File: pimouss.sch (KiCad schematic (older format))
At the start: 20 parts

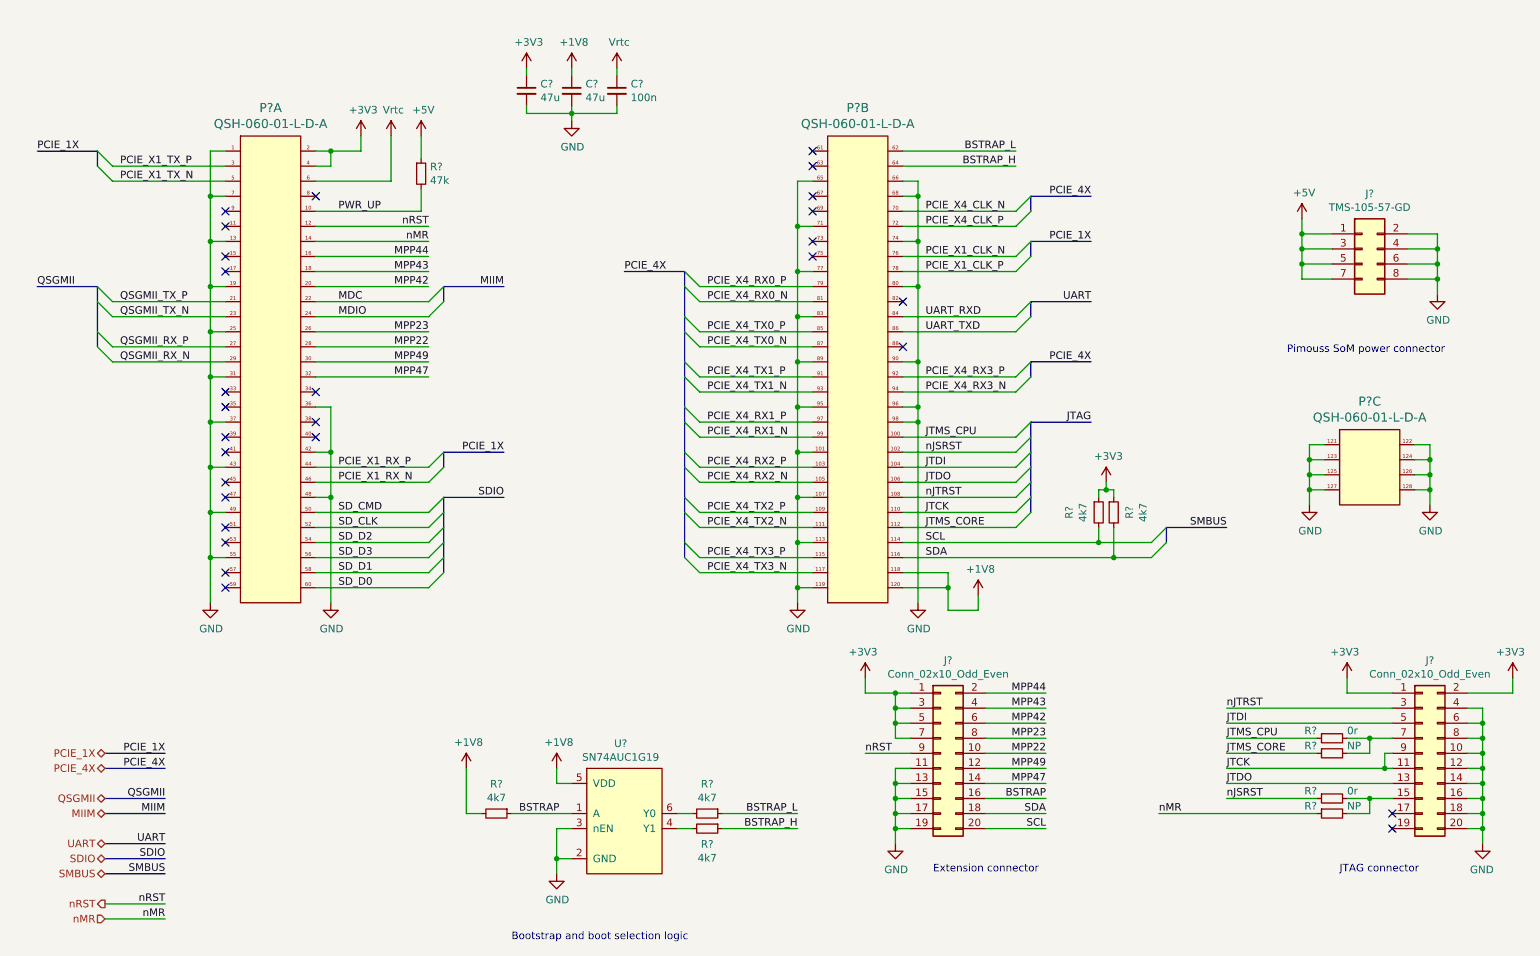
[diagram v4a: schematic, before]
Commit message: sch: Remove ALL busses since kicad's support is broken
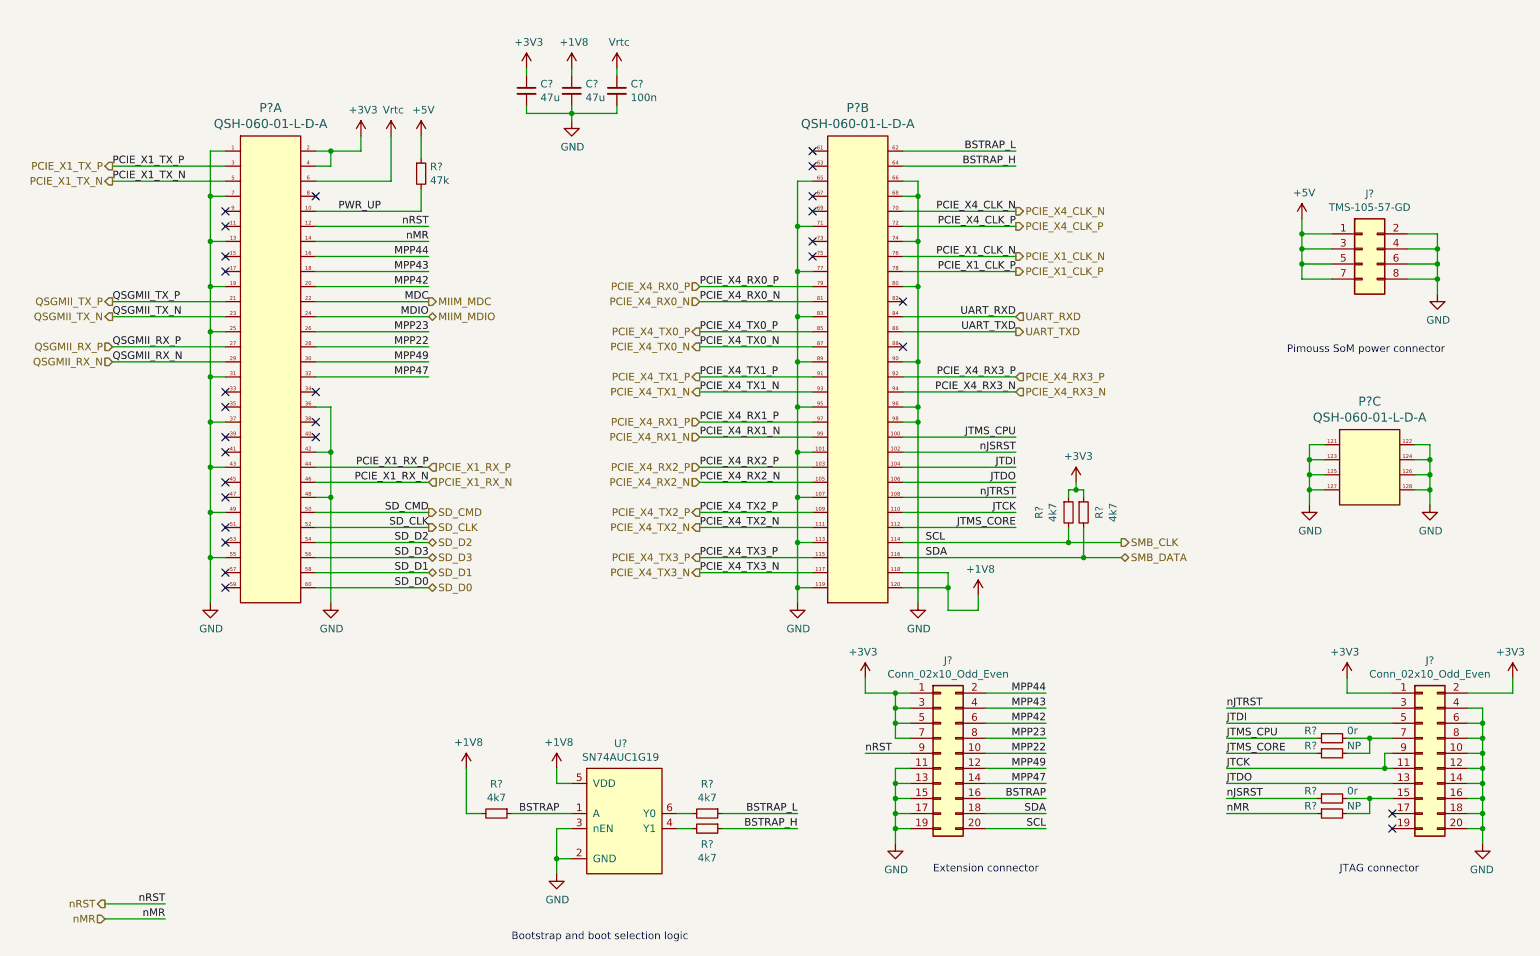
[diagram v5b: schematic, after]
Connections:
- net MDC renamed MIIM_MDC
- net MDIO renamed MIIM_MDIO
- net SCL renamed SMB_CLK
- net SDA renamed SMB_DATA
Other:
- moved on the sheet: R?

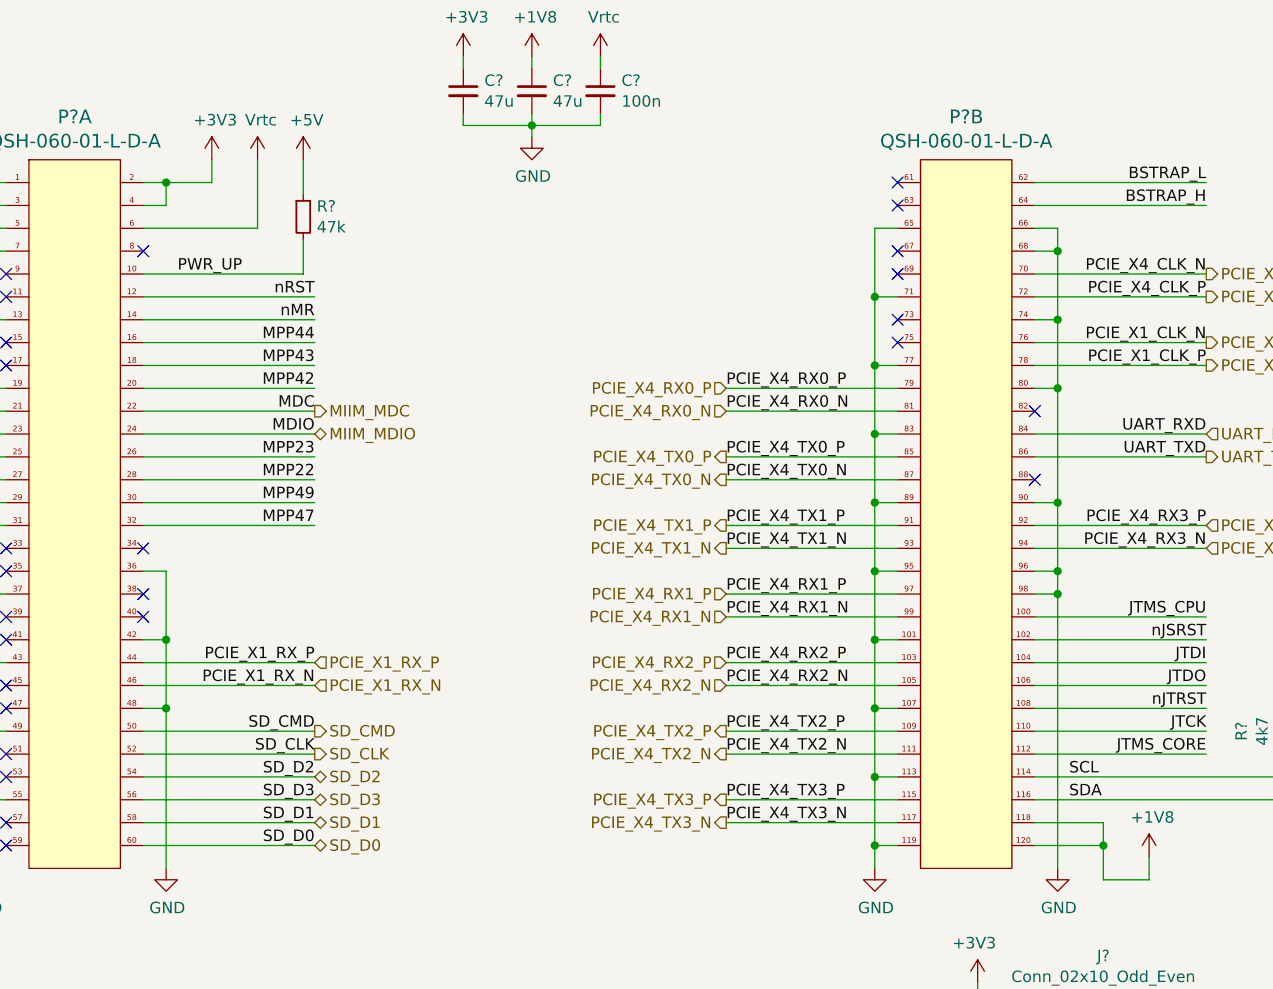
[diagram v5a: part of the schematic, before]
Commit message: sch: Make ERC happy with dummy power outputs
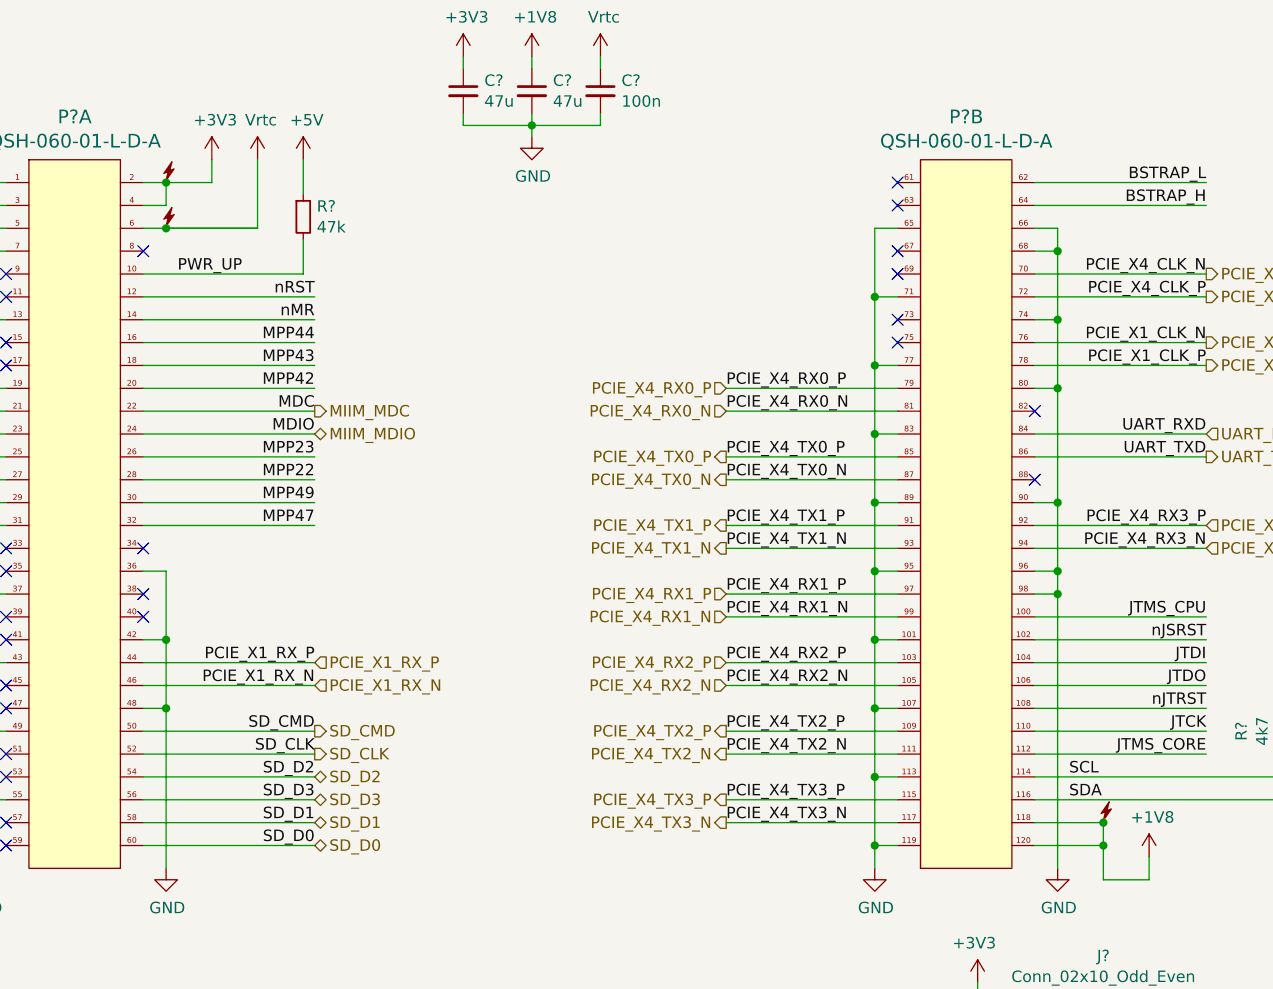
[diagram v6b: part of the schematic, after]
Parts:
- added DS? (x3): DummySupply, symbol pimouss-motherboard:DummySupply
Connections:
- net +1V8: now also DS?.~ (Dummy)
- net +3V3: now also DS?.~ (Dummy)
- net Vrtc: now also DS?.~ (Dummy)
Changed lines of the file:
@@
 Text HLabel 1550 1700 0    50   Output ~ 0
 PCIE_X1_TX_P
+$Comp
+L pimouss-motherboard:DummySupply DS?
+U 1 1 5DE0B5A3
+P 7100 4400
+AR Path="/5DE0B5A3" Ref="DS?"  Part="1"
+AR Path="/5CE77C37/5DE0B5A3" Ref="DS?"  Part="1"
+F 0 "DS?" H 7100 4400 50  0001 C CNN
+F 1 "DummySupply" H 7100 4400 50  0001 C CNN
+F 2 "" H 7100 4400 50  0001 C CNN
+F 3 "" H 7100 4400 50  0001 C CNN
+	1    7100 4400
+	1    0    0    -1
+$EndComp
+$Comp
+L pimouss-motherboard:DummySupply DS?
+U 1 1 5DE20D38
+P 3000 1800
+AR Path="/5DE20D38" Ref="DS?"  Part="1"
+AR Path="/5CE77C37/5DE20D38" Ref="DS?"  Part="1"
+F 0 "DS?" H 3000 1800 50  0001 C CNN
+F 1 "DummySupply" H 3000 1800 50  0001 C CNN
+F 2 "" H 3000 1800 50  0001 C CNN
+F 3 "" H 3000 1800 50  0001 C CNN
+	1    3000 1800
+	1    0    0    -1
+$EndComp
+$Comp
+L pimouss-motherboard:DummySupply DS?
+U 1 1 5DE48D70
+P 3000 1600
+AR Path="/5DE48D70" Ref="DS?"  Part="1"
+AR Path="/5CE77C37/5DE48D70" Ref="DS?"  Part="1"
+F 0 "DS?" H 3000 1600 50  0001 C CNN
+F 1 "DummySupply" H 3000 1600 50  0001 C CNN
+F 2 "" H 3000 1600 50  0001 C CNN
+F 3 "" H 3000 1600 50  0001 C CNN
+	1    3000 1600
+	1    0    0    -1
+$EndComp
+Connection ~ 3000 1800
+Wire Wire Line
+	3000 1800 3400 1800
+Connection ~ 7100 4400
 $EndSCHEMATC

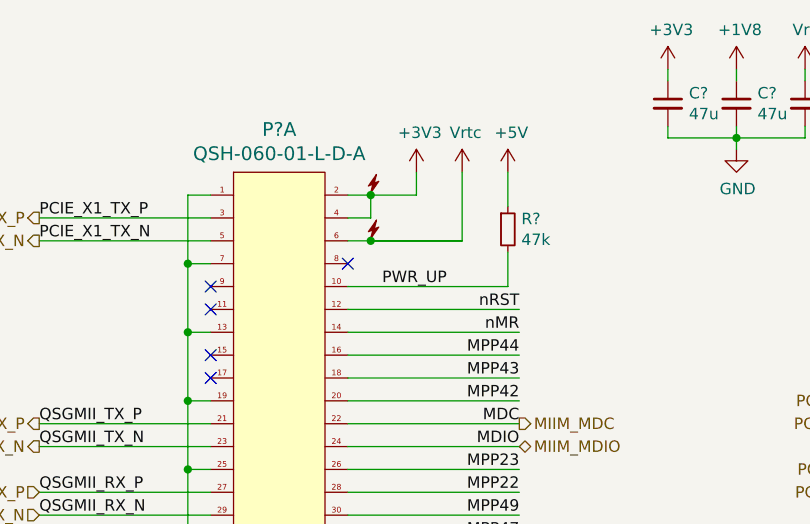
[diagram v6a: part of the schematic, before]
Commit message: lib, sch: Misc changes to make ERC happy
- add resistors to PCIe switch GPIOs
- add NC flags on PHY unused LED outputs
- add dummy supply on Earth PSU
- add dummy supply on PHY ref clock's VCC
- LTC3633: deduplicate SW1/2 outputs
- ILS8033: deduplicate LX1/2 and PGND1/2 outputs
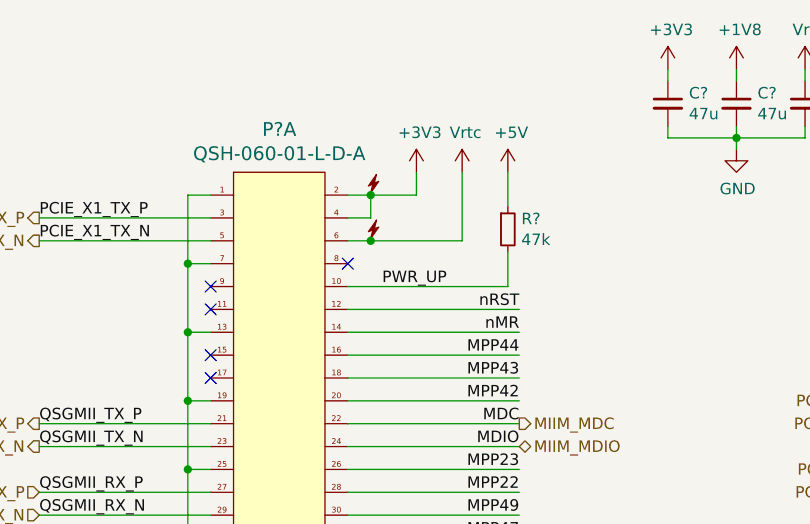
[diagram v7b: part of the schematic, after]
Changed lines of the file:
@@
 $EndComp
 Wire Wire Line
-	2900 1800 3400 1800
+	2900 1800 3000 1800
 Wire Wire Line
 	3400 1800 3400 1500

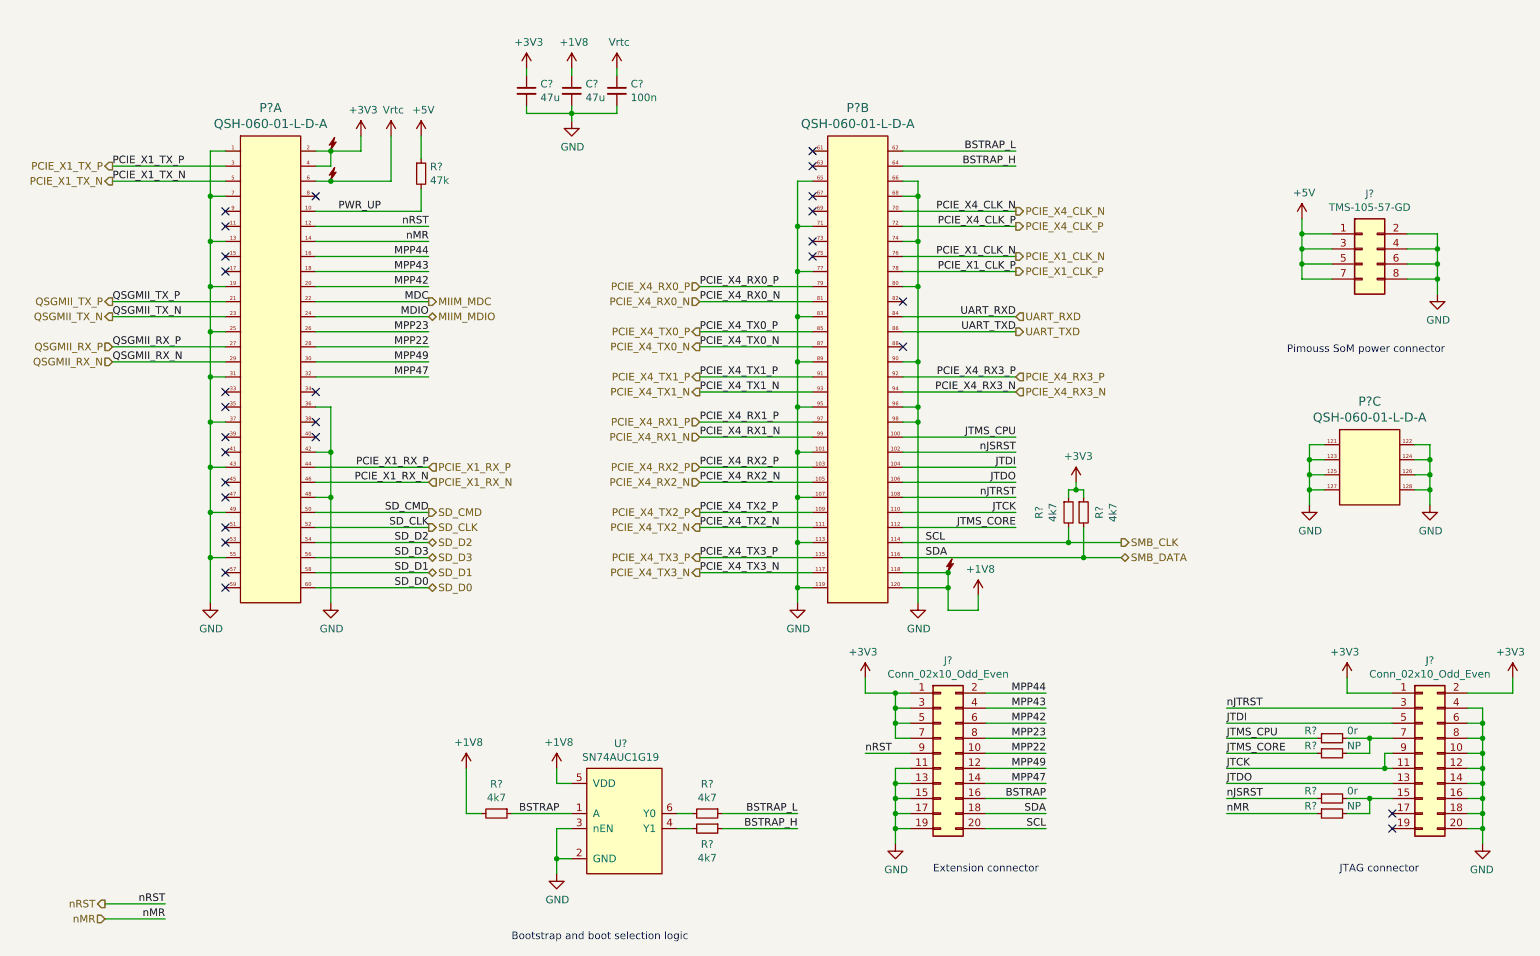
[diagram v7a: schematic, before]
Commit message: sch: Annotate & associate symbols with footprints
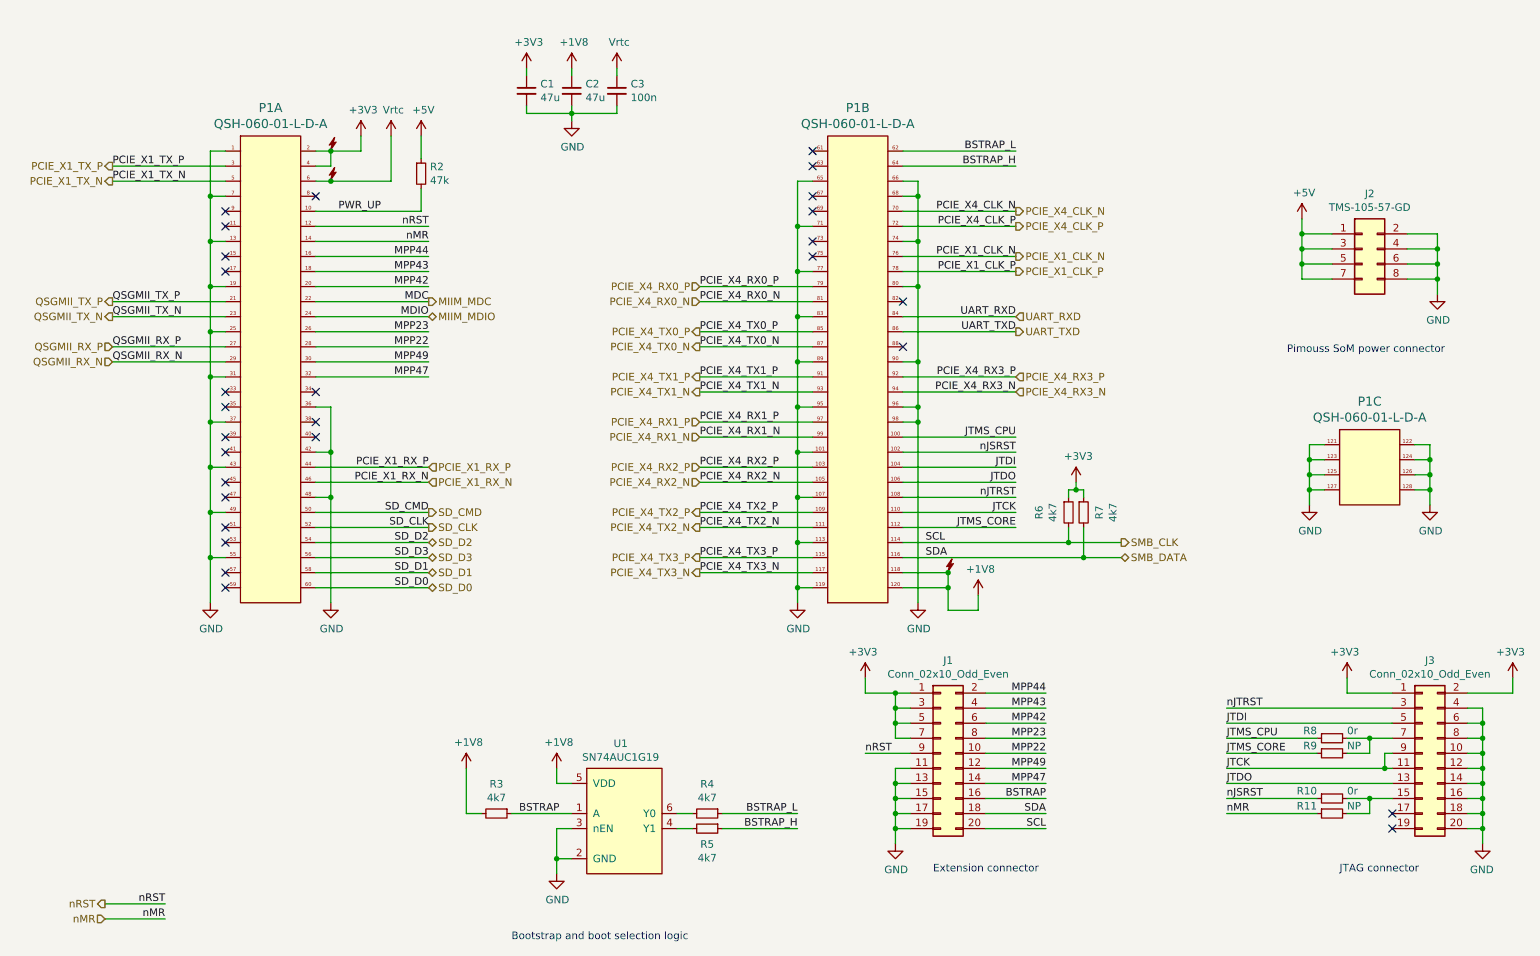
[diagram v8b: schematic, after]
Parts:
- removed DS? (x3): DummySupply, symbol pimouss-motherboard:DummySupply
- C1, C2: renamed from C?; footprint (none) -> Capacitor_SMD:C_0805_2012Metric
- C3: renamed from C?; footprint (none) -> Capacitor_SMD:C_0603_1608Metric
- J1, J3: renamed from J?; footprint (none) -> Connector_PinHeader_2.54mm:PinHeader_2x10_P2.54mm_Vertical
- R10, R11, R2, R3, R4, R5, R6, R7, R8, R9: renamed from R?; footprint (none) -> Resistor_SMD:R_0603_1608Metric
- gave numbers to parts that had none: 3
